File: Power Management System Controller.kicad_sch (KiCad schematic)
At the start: 0 parts

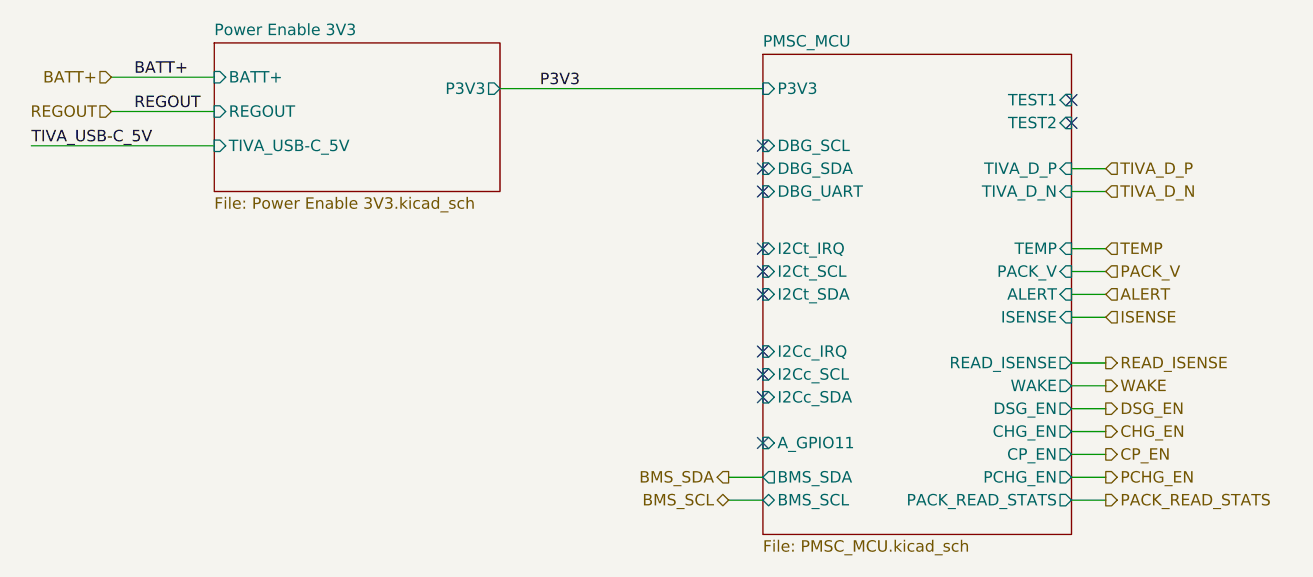
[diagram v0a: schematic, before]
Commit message: commit before simplifying and removing features
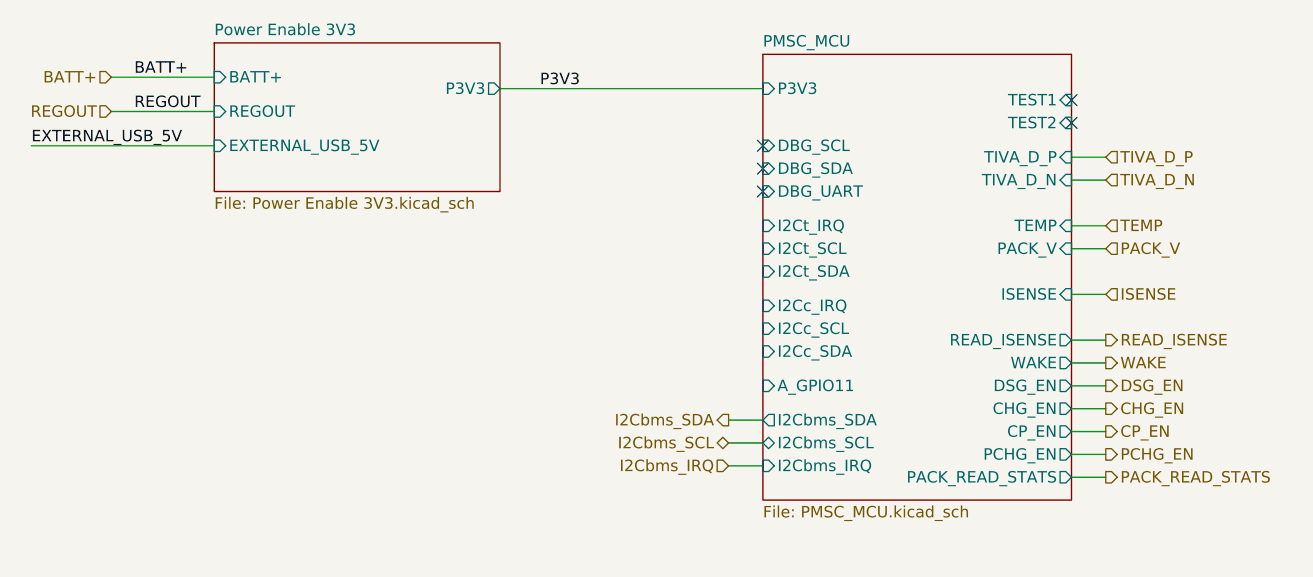
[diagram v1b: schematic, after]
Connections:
- no-connect marks 12 -> 5
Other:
- sheet PMSC_MCU ports: added I2Cbms_IRQ, I2Cbms_SCL, I2Cbms_SDA; removed ALERT, BMS_SCL, BMS_SDA
- sheet Power Enable 3V3 ports: added EXTERNAL_USB_5V; removed TIVA_USB-C_5V
